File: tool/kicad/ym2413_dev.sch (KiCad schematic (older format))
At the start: 147 parts, among them IC1 6N135, J1 MICRO-USB-AB, K1 CONN_3, K2 CONN_3, P1 TEST_POINT, P10 TEST_POINT, P11 TEST_POINT, P12 TEST_POINT, P13 TEST_POINT, P14 TEST_POINT, P15 TEST_POINT, P16 TEST_POINT, P17 TEST_POINT, P18 TEST_POINT, P19 TEST_POINT, P2 TEST_POINT, P20 TEST_POINT, P21 TEST_POINT, P22 TEST_POINT, P23 TEST_POINT, P24 TEST_POINT, P25 TEST_POINT, P26 TEST_POINT, P27 TEST_POINT, P28 TEST_POINT, P29 TEST_POINT, P3 TEST_POINT, P30 CONN_3X2, P31 CONN_2, P32 CONN_2, P33 TEST_POINT, P34 TEST_POINT, P35 CONN_6, P36 CONN_5, P37 TEST_POINT, P38 TEST_POINT, P4 TEST_POINT, P5 MIDI-IN, P6 TEST_POINT, P7 TEST_POINT, P8 TEST_POINT, P9 TEST_POINT, U1 SN74LVC2T45, U2 ST-USBLC6-2, U3 EFM32GG332, U4 YM2413, U5 LM386, U6 LM386, X1 48Mhz, X2 CRYSTAL

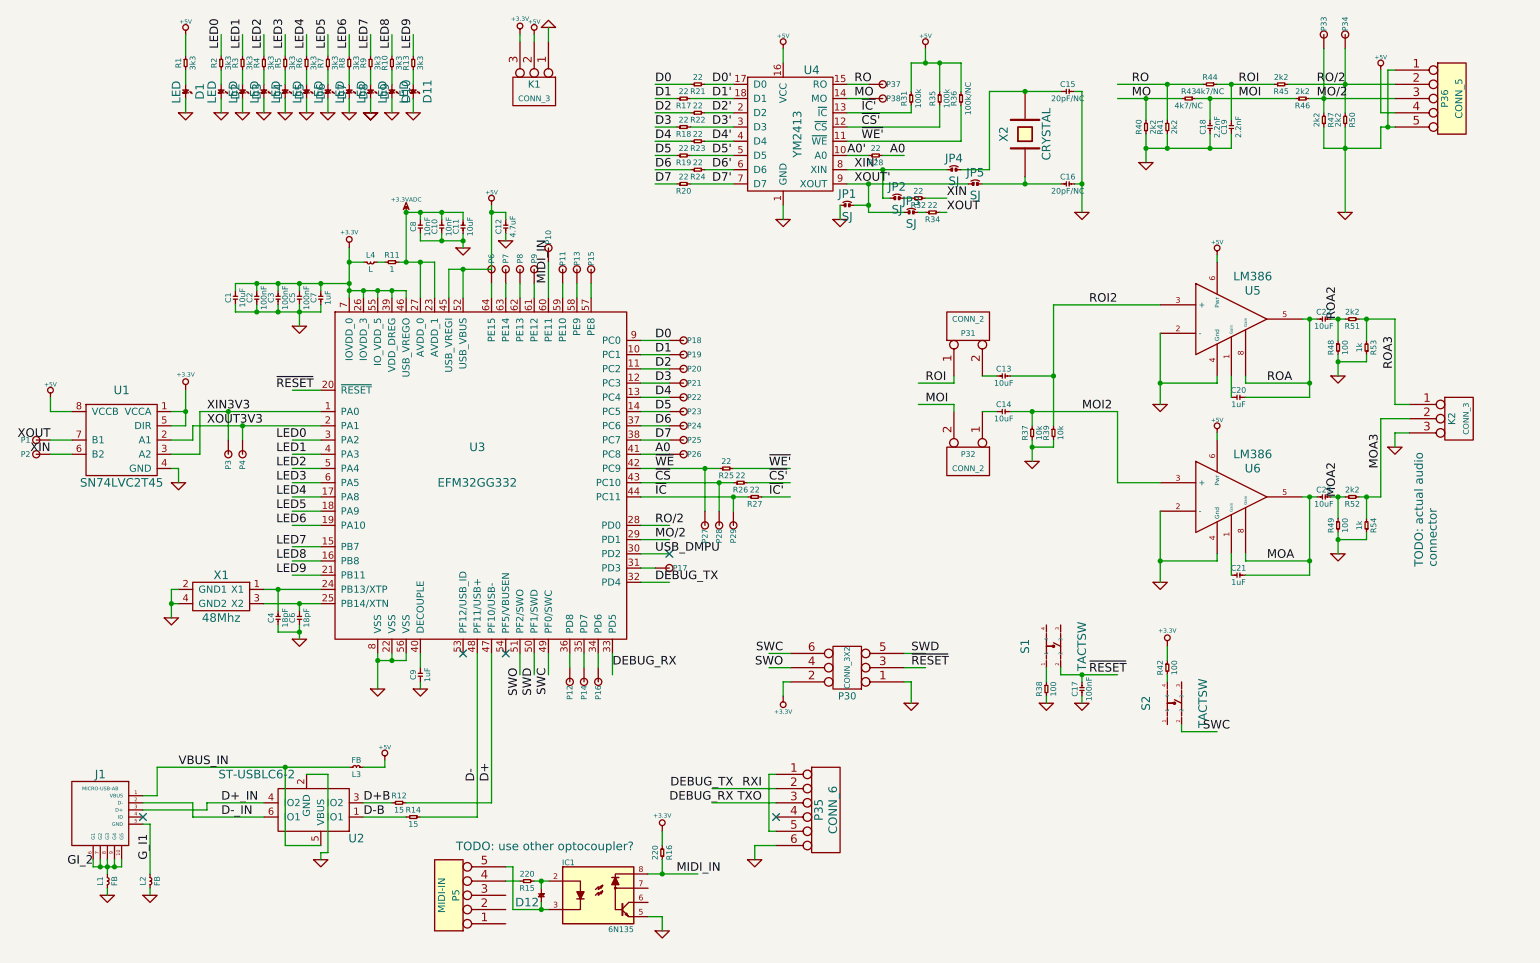
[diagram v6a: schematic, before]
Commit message: fix used optocoupler
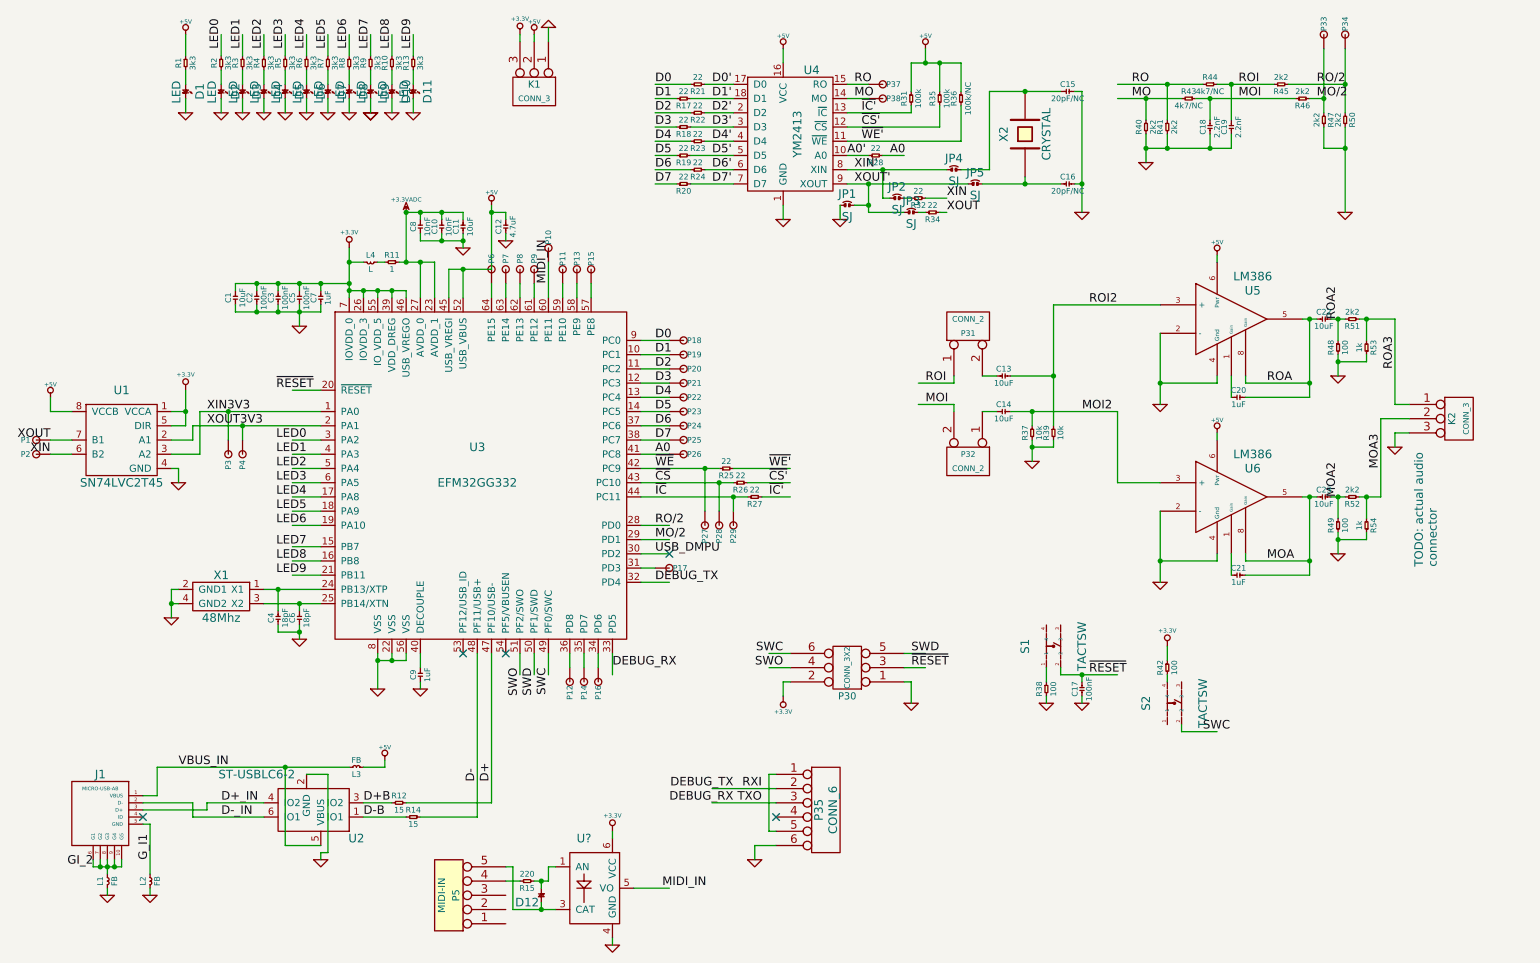
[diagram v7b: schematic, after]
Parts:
- removed IC1: 6N135, symbol 6N135
- removed P36: CONN_5, symbol CONN_5
- removed R16: 220, symbol R
- added U?: ACPL-M21L, symbol ACPL-M21L
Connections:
- wire segments 362 -> 356
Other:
- note removed: "TODO: use other optocoupler?"

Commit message: latest
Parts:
- gave numbers to parts that had none: 1
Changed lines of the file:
@@
 	6850 2400 6800 2400
 $Comp
-L GND #PWR034
+L GND #PWR032
 U 1 1 52F7930D
 P 6500 2550
-F 0 "#PWR034" H 6500 2550 30  0001 C CNN
+F 0 "#PWR032" H 6500 2550 30  0001 C CNN
 F 1 "GND" H 6500 2480 30  0001 C CNN
 F 2 "" H 6500 2550 60  0000 C CNN
@@
 	8800 5750 8800 5800
 $Comp
-L +3.3V #PWR035
+L +3.3V #PWR033
 U 1 1 52F79B5B
 P 8800 5550
-F 0 "#PWR035" H 8800 5510 30  0001 C CNN
+F 0 "#PWR033" H 8800 5510 30  0001 C CNN
 F 1 "+3.3V" H 8800 5660 30  0000 C CNN
 F 2 "" H 8800 5550 60  0000 C CNN
@@
 	10300 3950 10500 3950
 $Comp
-L GND #PWR036
+L GND #PWR034
 U 1 1 52F7A44E
 P 10400 4150
-F 0 "#PWR036" H 10400 4150 30  0001 C CNN
+F 0 "#PWR034" H 10400 4150 30  0001 C CNN
 F 1 "GND" H 10400 4080 30  0001 C CNN
 F 2 "" H 10400 4150 60  0000 C CNN
@@
 $EndComp
 $Comp
-L +3.3V #PWR037
+L +3.3V #PWR035
 U 1 1 52F7A870
 P 1900 3750
-F 0 "#PWR037" H 1900 3710 30  0001 C CNN
+F 0 "#PWR035" H 1900 3710 30  0001 C CNN
 F 1 "+3.3V" H 1900 3860 30  0000 C CNN
 F 2 "" H 1900 3750 60  0000 C CNN
@@
 	950  3900 950  3800
 $Comp
-L +5V #PWR038
+L +5V #PWR036
 U 1 1 52F7B2D9
 P 950 3800
-F 0 "#PWR038" H 950 3890 20  0001 C CNN
+F 0 "#PWR036" H 950 3890 20  0001 C CNN
 F 1 "+5V" H 950 3890 30  0000 C CNN
 F 2 "" H 950 3800 60  0000 C CNN
@@
 	1900 1800 1900 1700
 $Comp
-L GND #PWR039
+L GND #PWR037
 U 1 1 52F7ED33
 P 1900 1800
-F 0 "#PWR039" H 1900 1800 30  0001 C CNN
+F 0 "#PWR037" H 1900 1800 30  0001 C CNN
 F 1 "GND" H 1900 1730 30  0001 C CNN
 F 2 "" H 1900 1800 60  0000 C CNN
@@
 	2150 1800 2150 1700
 $Comp
-L GND #PWR040
+L GND #PWR038
 U 1 1 52F7EEC5
 P 2150 1800
-F 0 "#PWR040" H 2150 1800 30  0001 C CNN
+F 0 "#PWR038" H 2150 1800 30  0001 C CNN
 F 1 "GND" H 2150 1730 30  0001 C CNN
 F 2 "" H 2150 1800 60  0000 C CNN
@@
 	2300 1800 2300 1700
 $Comp
-L GND #PWR041
+L GND #PWR039
 U 1 1 52F7EEDA
 P 2300 1800
-F 0 "#PWR041" H 2300 1800 30  0001 C CNN
+F 0 "#PWR039" H 2300 1800 30  0001 C CNN
 F 1 "GND" H 2300 1730 30  0001 C CNN
 F 2 "" H 2300 1800 60  0000 C CNN
@@
 	2450 1800 2450 1700
 $Comp
-L GND #PWR042
+L GND #PWR040
 U 1 1 52F7EEEF
 P 2450 1800
-F 0 "#PWR042" H 2450 1800 30  0001 C CNN
+F 0 "#PWR040" H 2450 1800 30  0001 C CNN
 F 1 "GND" H 2450 1730 30  0001 C CNN
 F 2 "" H 2450 1800 60  0000 C CNN
@@
 	2600 1800 2600 1700
 $Comp
-L GND #PWR043
+L GND #PWR041
 U 1 1 52F7EF04
 P 2600 1800
-F 0 "#PWR043" H 2600 1800 30  0001 C CNN
+F 0 "#PWR041" H 2600 1800 30  0001 C CNN
 F 1 "GND" H 2600 1730 30  0001 C CNN
 F 2 "" H 2600 1800 60  0000 C CNN
@@
 	2750 1800 2750 1700
 $Comp
-L GND #PWR044
+L GND #PWR042
 U 1 1 52F7EF19
 P 2750 1800
-F 0 "#PWR044" H 2750 1800 30  0001 C CNN
+F 0 "#PWR042" H 2750 1800 30  0001 C CNN
 F 1 "GND" H 2750 1730 30  0001 C CNN
 F 2 "" H 2750 1800 60  0000 C CNN
@@
 	2900 1800 2900 1700
 $Comp
-L GND #PWR045
+L GND #PWR043
 U 1 1 52F7EF2E
 P 2900 1800
-F 0 "#PWR045" H 2900 1800 30  0001 C CNN
+F 0 "#PWR043" H 2900 1800 30  0001 C CNN
 F 1 "GND" H 2900 1730 30  0001 C CNN
 F 2 "" H 2900 1800 60  0000 C CNN
@@
 	3050 1800 3050 1700
 $Comp
-L GND #PWR046
+L GND #PWR044
 U 1 1 52F7EF43
 P 3050 1800
-F 0 "#PWR046" H 3050 1800 30  0001 C CNN
+F 0 "#PWR044" H 3050 1800 30  0001 C CNN
 F 1 "GND" H 3050 1730 30  0001 C CNN
 F 2 "" H 3050 1800 60  0000 C CNN
@@
 	3200 1800 3200 1700
 $Comp
-L GND #PWR047
+L GND #PWR045
 U 1 1 52F7EF58
 P 3200 1800
-F 0 "#PWR047" H 3200 1800 30  0001 C CNN
+F 0 "#PWR045" H 3200 1800 30  0001 C CNN
 F 1 "GND" H 3200 1730 30  0001 C CNN
 F 2 "" H 3200 1800 60  0000 C CNN
@@
 	3200 1250 3200 1400
 $Comp
-L GND #PWR048
+L GND #PWR046
 U 1 1 52F7EF5F
 P 3200 1800
-F 0 "#PWR048" H 3200 1800 30  0001 C CNN
+F 0 "#PWR046" H 3200 1800 30  0001 C CNN
 F 1 "GND" H 3200 1730 30  0001 C CNN
 F 2 "" H 3200 1800 60  0000 C CNN
@@
 	3350 1800 3350 1700
 $Comp
-L GND #PWR049
+L GND #PWR047
 U 1 1 52F7EF73
 P 3350 1800
-F 0 "#PWR049" H 3350 1800 30  0001 C CNN
+F 0 "#PWR047" H 3350 1800 30  0001 C CNN
 F 1 "GND" H 3350 1730 30  0001 C CNN
 F 2 "" H 3350 1800 60  0000 C CNN
@@
 	3500 1800 3500 1700
 $Comp
-L GND #PWR050
+L GND #PWR048
 U 1 1 52F7EF88
 P 3500 1800
-F 0 "#PWR050" H 3500 1800 30  0001 C CNN
+F 0 "#PWR048" H 3500 1800 30  0001 C CNN
 F 1 "GND" H 3500 1730 30  0001 C CNN
 F 2 "" H 3500 1800 60  0000 C CNN
@@
 	3500 1250 3500 1400
 $Comp
-L +5V #PWR051
+L +5V #PWR049
 U 1 1 52F7EF8F
 P 1900 1250
-F 0 "#PWR051" H 1900 1340 20  0001 C CNN
+F 0 "#PWR049" H 1900 1340 20  0001 C CNN
 F 1 "+5V" H 1900 1340 30  0000 C CNN
 F 2 "" H 1900 1250 60  0000 C CNN
@@
 $EndComp
 $Comp
-L GND #PWR052
+L GND #PWR050
 U 1 1 52F821C2
 P 4450 1200
-F 0 "#PWR052" H 4450 1200 30  0001 C CNN
+F 0 "#PWR050" H 4450 1200 30  0001 C CNN
 F 1 "GND" H 4450 1130 30  0001 C CNN
 F 2 "" H 4450 1200 60  0000 C CNN
@@
 $EndComp
 $Comp
-L +5V #PWR053
+L +5V #PWR051
 U 1 1 52F821C8
 P 4350 1250
-F 0 "#PWR053" H 4350 1340 20  0001 C CNN
+F 0 "#PWR051" H 4350 1340 20  0001 C CNN
 F 1 "+5V" H 4350 1340 30  0000 C CNN
 F 2 "" H 4350 1250 60  0000 C CNN
@@
 $EndComp
 $Comp
-L +3.3V #PWR054
+L +3.3V #PWR052
 U 1 1 52F821CE
 P 4250 1250
-F 0 "#PWR054" H 4250 1210 30  0001 C CNN
+F 0 "#PWR052" H 4250 1210 30  0001 C CNN
 F 1 "+3.3V" H 4250 1360 30  0000 C CNN
 F 2 "" H 4250 1250 60  0000 C CNN
@@
 	5900 6950 6050 6950
 $Comp
-L GND #PWR055
+L GND #PWR053
 U 1 1 52F8750B
 P 5900 7050
-F 0 "#PWR055" H 5900 7050 30  0001 C CNN
+F 0 "#PWR053" H 5900 7050 30  0001 C CNN
 F 1 "GND" H 5900 6980 30  0001 C CNN
 F 2 "" H 5900 7050 60  0000 C CNN
@@
 	1950 4100 1800 4100
 $Comp
-L GND #PWR056
+L GND #PWR054
 U 1 1 52F8A394
 P 1850 4400
-F 0 "#PWR056" H 1850 4400 30  0001 C CNN
+F 0 "#PWR054" H 1850 4400 30  0001 C CNN
 F 1 "GND" H 1850 4330 30  0001 C CNN
 F 2 "" H 1850 4400 60  0000 C CNN
@@
 	10050 2050 9900 2050
 $Comp
-L ACPL-M21L U?
+L ACPL-M21L U7
 U 1 1 52F8C674
 P 4900 7300
-F 0 "U?" H 4700 7700 60  0000 C CNN
+F 0 "U7" H 4700 7700 60  0000 C CNN
 F 1 "ACPL-M21L" H 4550 7050 60  0001 C CNN
 F 2 "" H 4900 7300 60  0000 C CNN
@@
 	4450 7100 4450 7200
 $Comp
-L GND #PWR?
+L GND #PWR055
 U 1 1 52F8C9F7
 P 4900 7650
-F 0 "#PWR?" H 4900 7650 30  0001 C CNN
+F 0 "#PWR055" H 4900 7650 30  0001 C CNN
 F 1 "GND" H 4900 7580 30  0001 C CNN
 F 2 "" H 4900 7650 60  0000 C CNN
@@
 	4900 7600 4900 7650
 $Comp
-L +3.3V #PWR?
+L +3.3V #PWR056
 U 1 1 52F8CBAF
 P 4900 6850
-F 0 "#PWR?" H 4900 6810 30  0001 C CNN
+F 0 "#PWR056" H 4900 6810 30  0001 C CNN
 F 1 "+3.3V" H 4900 6960 30  0000 C CNN
 F 2 "" H 4900 6850 60  0000 C CNN
